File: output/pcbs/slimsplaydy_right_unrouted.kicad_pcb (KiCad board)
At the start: 2 copper layers, 122.9 x 94.7 mm, 42 parts

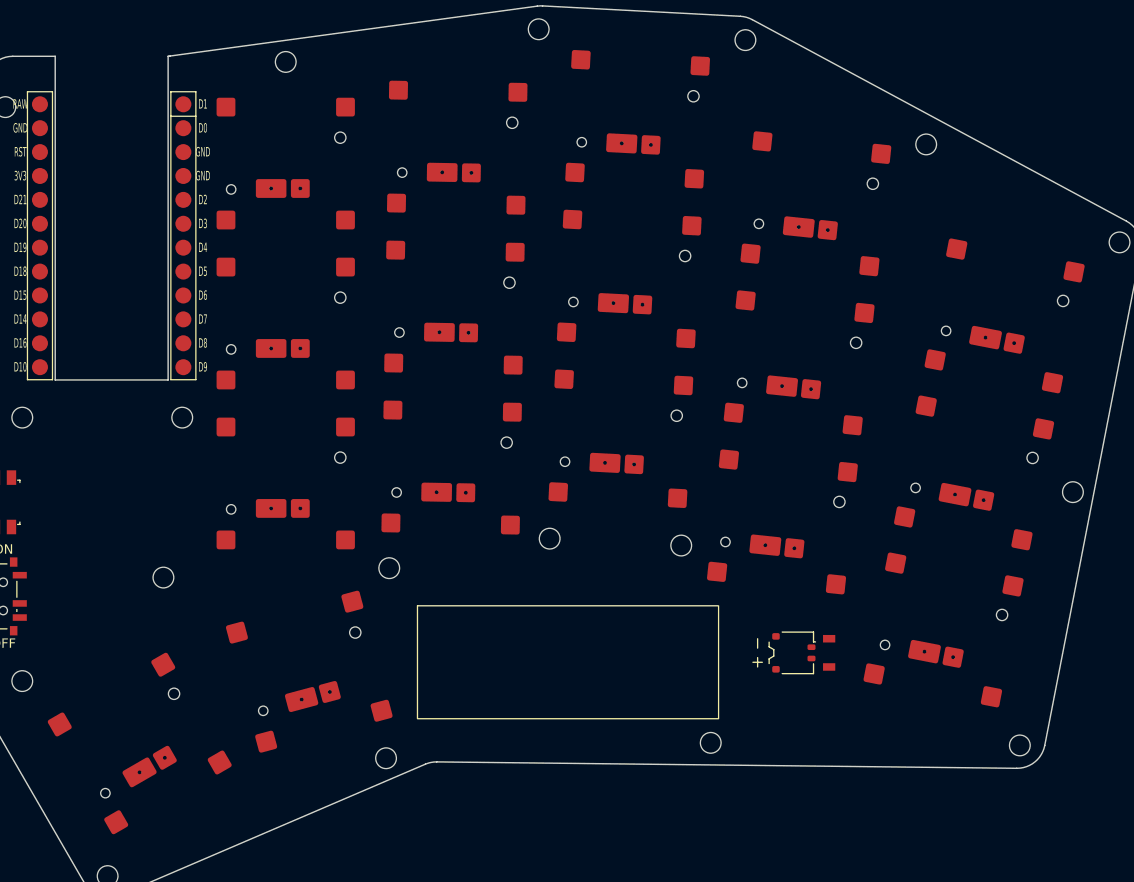
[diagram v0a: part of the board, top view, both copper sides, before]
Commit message: Add via holesize options separate from via size options.
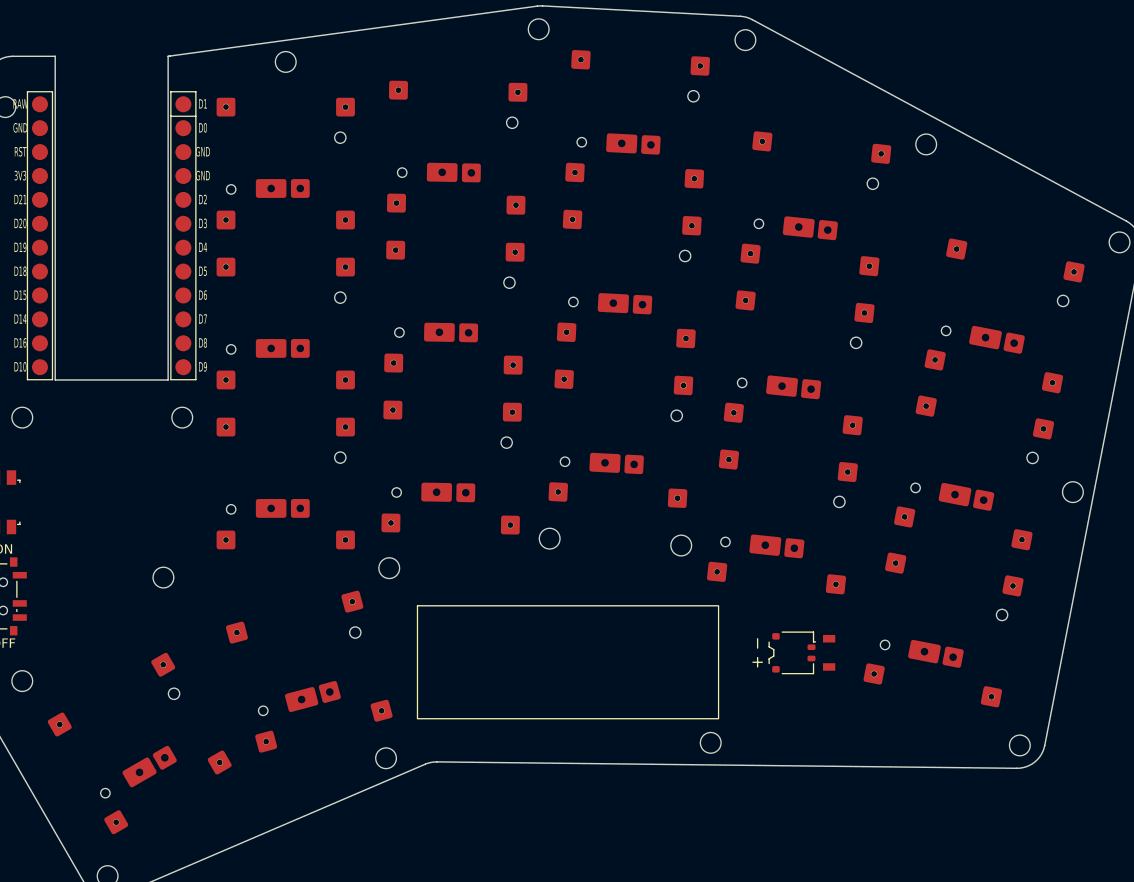
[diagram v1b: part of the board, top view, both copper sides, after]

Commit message: Finish layout, schematic, routing.
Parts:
- removed MH16, MH17, MH18: , ceoloide:mounting_hole_npth
- removed PAD1, PAD2: , SMDPad
- removed XX1: , Battery_301230
- added MAG1: , magsafe, B.Cu at (179.9, -32.5)
- CONN1: footprint ceoloide:battery_connector_molex_pico_ezmate_1x02 -> Molex_Pico_EZMate_Plus_1x02
- moved MH15 245.8 mm to (163.9, -60.5), turned to 0 degrees
- moved MH5 228.6 mm to (123.4, -55.5)
- moved MH13 219.9 mm to (240.9, -42.7), turned to -8 degrees
- moved MH14 216.9 mm to (222.0, -51.8), turned to -3 degrees
- moved MH8 208.3 mm to (123.9, 8.55), turned to 0 degrees
- moved CONN1 200.6 mm to (184.9, -8.45), turned to 0 degrees
- moved MH4 196.4 mm to (147.9, -57.8)
- moved MH6 195.1 mm to (134.9, -21.5)
- moved MH7 194.8 mm to (142.4, 0.55), turned to 0 degrees
- moved MH3 193.5 mm to (189.9, -64.8)
- moved S6 179.7 mm to (209.8, -47.4), turned to -3 degrees
- moved S5 179.1 mm to (208.9, -30.5), turned to -3 degrees
- moved S9 178.7 mm to (189.9, -54.5), turned to 0 degrees
- moved S4 178.5 mm to (208.0, -13.5), turned to -3 degrees
- moved S3 178.3 mm to (229.7, -33.7), turned to -8 degrees
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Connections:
- MCU1 pad 1: mirror_hand_middle_top -> mirror_finger_inner_home
- MCU1 pad 10: mirror_hand_inner_home -> mirror_finger_pinky_top
- MCU1 pad 11: mirror_hand_ring_home -> mirror_thumb_tucky_fan
- MCU1 pad 12: mirror_hand_pinky_home -> mirror_thumb_reachy_fan
- MCU1 pad 13: mirror_hand_pinky_bottom -> mirror_finger_index_home
- MCU1 pad 14: mirror_hand_middle_bottom -> mirror_finger_middle_home
- MCU1 pad 15: mirror_hand_index_bottom -> mirror_finger_ring_home
- MCU1 pad 16: mirror_hand_inner_bottom -> mirror_finger_pinky_home
- MCU1 pad 17: mirror_hand_ring_bottom -> mirror_finger_ring_top
- MCU1 pad 18: mirror_thumb_near_fan -> mirror_finger_middle_top
- MCU1 pad 19: mirror_thumb_far_fan -> mirror_finger_index_top
- MCU1 pad 2: mirror_hand_index_top -> D0
- MCU1 pad 20: D21 -> mirror_finger_inner_top
- MCU1 pad 5: mirror_hand_inner_top -> mirror_finger_pinky_bottom
- MCU1 pad 6: mirror_hand_ring_top -> mirror_finger_ring_bottom
- MCU1 pad 7: mirror_hand_pinky_top -> mirror_finger_middle_bottom
- MCU1 pad 8: mirror_hand_middle_home -> mirror_finger_index_bottom
- MCU1 pad 9: mirror_hand_index_home -> mirror_finger_inner_bottom
- S1 pad : GND -> (no net)
- S1 pad 1: mirror_hand_pinky_bottom -> mirror_finger_pinky_bottom
- S1 pad 3: (no net) -> GND
- S10 pad : GND -> (no net)
- S10 pad 1: mirror_hand_index_bottom -> mirror_finger_index_bottom
- S10 pad 3: (no net) -> GND
- S11 pad : GND -> (no net)
- S11 pad 1: mirror_hand_index_home -> mirror_finger_index_home
- S11 pad 3: (no net) -> GND
- S12 pad : GND -> (no net)
- S12 pad 1: mirror_hand_index_top -> mirror_finger_index_top
- S12 pad 3: (no net) -> GND
- S13 pad : GND -> (no net)
- S13 pad 1: mirror_hand_inner_bottom -> mirror_finger_inner_bottom
- S13 pad 3: (no net) -> GND
- S14 pad : GND -> (no net)
- S14 pad 1: mirror_hand_inner_home -> mirror_finger_inner_home
- S14 pad 3: (no net) -> GND
- S15 pad : GND -> (no net)
- S15 pad 1: mirror_hand_inner_top -> mirror_finger_inner_top
- S15 pad 3: (no net) -> GND
- S16 pad : GND -> (no net)
- S16 pad 1: mirror_thumb_near_fan -> mirror_thumb_tucky_fan
- S16 pad 3: (no net) -> GND
- S17 pad : GND -> (no net)
- S17 pad 1: mirror_thumb_far_fan -> mirror_thumb_reachy_fan
- S17 pad 3: (no net) -> GND
- S2 pad : GND -> (no net)
- S2 pad 1: mirror_hand_pinky_home -> mirror_finger_pinky_home
- S2 pad 3: (no net) -> GND
- S3 pad : GND -> (no net)
- S3 pad 1: mirror_hand_pinky_top -> mirror_finger_pinky_top
- S3 pad 3: (no net) -> GND
- S4 pad : GND -> (no net)
- S4 pad 1: mirror_hand_ring_bottom -> mirror_finger_ring_bottom
- S4 pad 3: (no net) -> GND
- S5 pad : GND -> (no net)
- S5 pad 1: mirror_hand_ring_home -> mirror_finger_ring_home
- S5 pad 3: (no net) -> GND
- S6 pad : GND -> (no net)
- S6 pad 1: mirror_hand_ring_top -> mirror_finger_ring_top
- S6 pad 3: (no net) -> GND
- S7 pad : GND -> (no net)
- S7 pad 1: mirror_hand_middle_bottom -> mirror_finger_middle_bottom
- S7 pad 3: (no net) -> GND
- S8 pad : GND -> (no net)
- S8 pad 1: mirror_hand_middle_home -> mirror_finger_middle_home
- S8 pad 3: (no net) -> GND
- S9 pad : GND -> (no net)
- S9 pad 1: mirror_hand_middle_top -> mirror_finger_middle_top
- S9 pad 3: (no net) -> GND
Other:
- board size 122.9 x 94.7 mm -> 122.6 x 97.5 mm

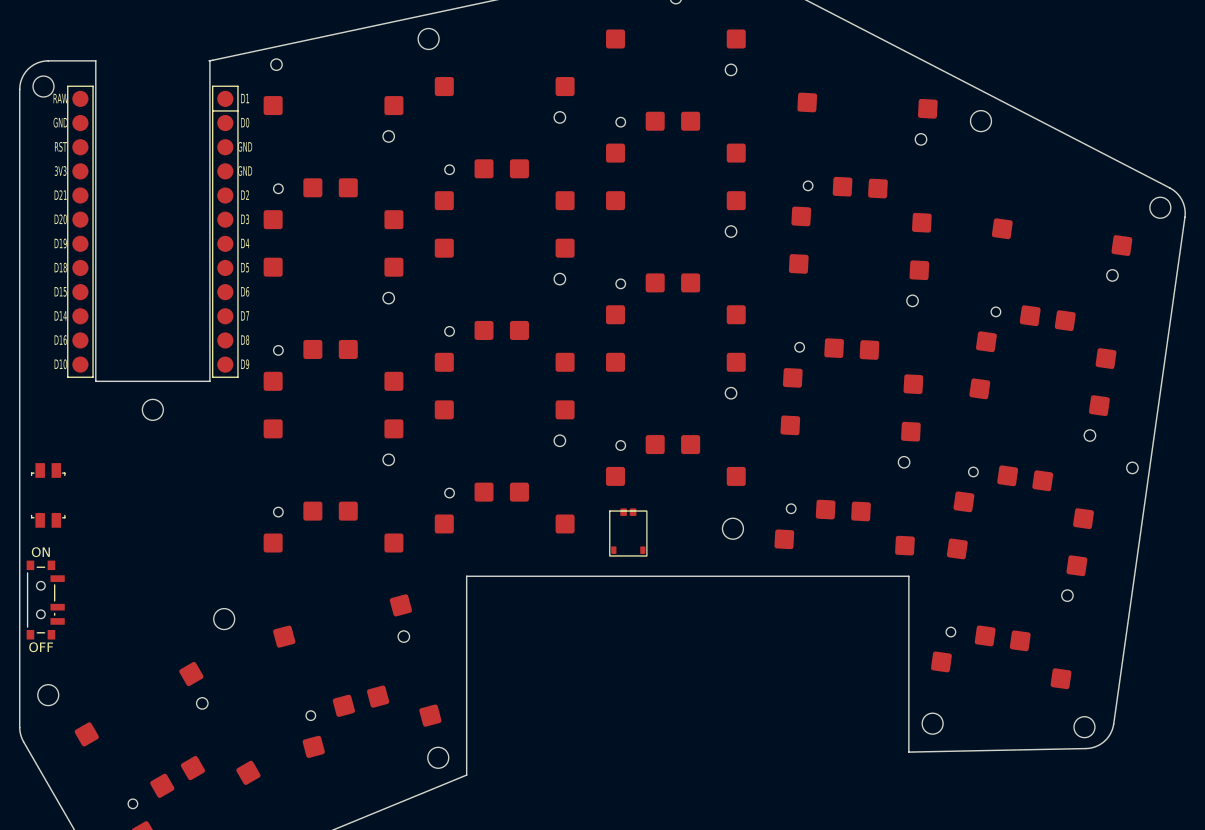
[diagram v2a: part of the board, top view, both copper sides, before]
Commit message: Fix MCU slots. Fillet outline. Reroute both sides. Re-re-reroute both sides.
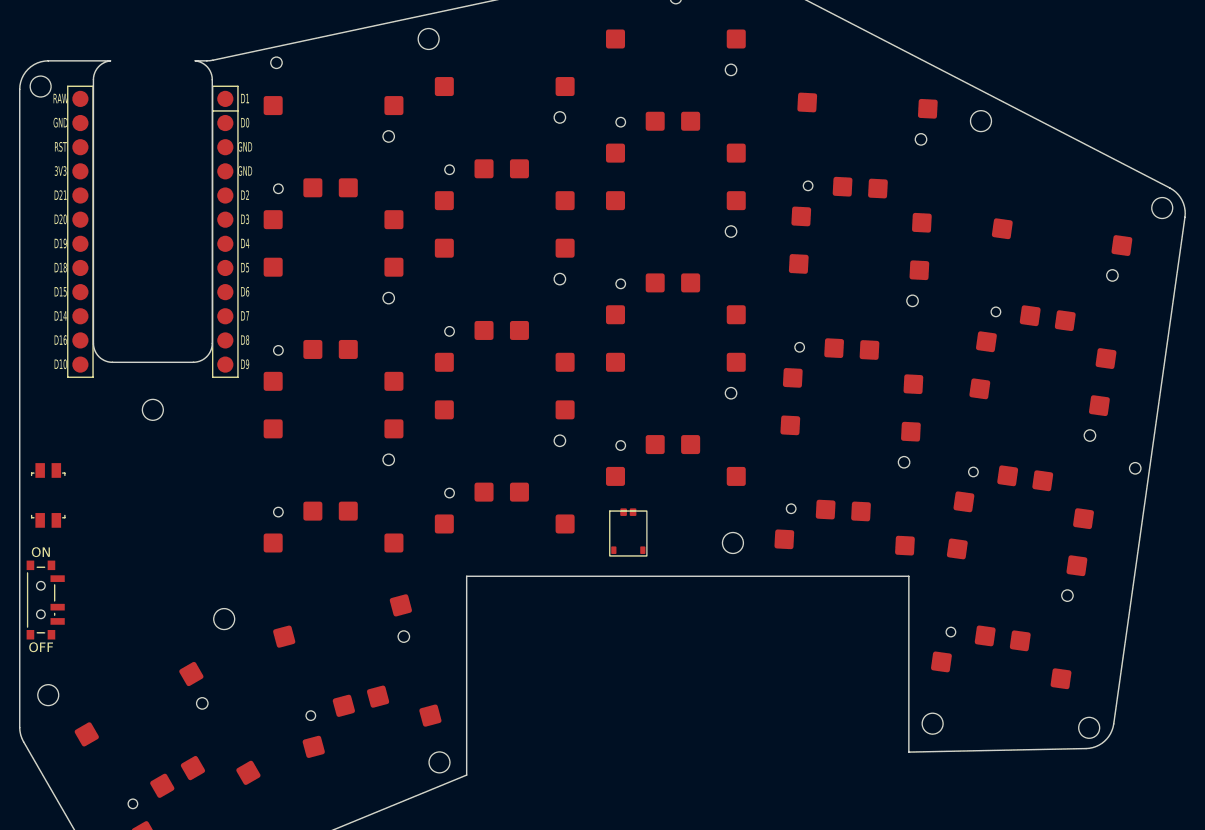
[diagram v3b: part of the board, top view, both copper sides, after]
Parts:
- moved MH10 1.50 mm to (195.9, -7.45)
- moved MH9 0.50 mm to (165.1, 15.6)
- moved MH12 0.50 mm to (233.4, 12.0)
- moved MH2 0.30 mm to (238.3, -15.3)
- moved MH5 0.30 mm to (123.1, -55.5)
- moved MH4 0.20 mm to (147.9, -58.0)
- moved MH13 0.20 mm to (241.1, -42.7)
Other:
- outline, holes or cut-outs redrawn
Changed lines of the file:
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@@
   (title_block
     (title "slimsplaydy_right_unrouted")
-    (date "2025-06-13")
+    (date "2025-06-14")
     (rev "0.1")
     (company "huntercook")
@@
   (footprint "ceoloide:mounting_hole_npth"
     (layer "F.Cu")
-    (at 237.95889780000002 -15.345405 -8)
+    (at 238.2559783 -15.303653099999998 -8)
     (property "Reference" "MH2"
       (at 0 2.55 -8)
@@
   (footprint "ceoloide:mounting_hole_npth"
     (layer "F.Cu")
-    (at 147.9492103 -57.7502446 0)
+    (at 147.9492103 -57.950244600000005 0)
     (property "Reference" "MH4"
       (at 0 2.55 0)
@@
   (footprint "ceoloide:mounting_hole_npth"
     (layer "F.Cu")
-    (at 123.4492103 -55.450244600000005 0)
+    (at 123.14921030000001 -55.450244600000005 0)
     (property "Reference" "MH5"
       (at 0 2.55 0)
@@
   (footprint "ceoloide:mounting_hole_npth"
     (layer "F.Cu")
-    (at 164.96236520000002 15.139062299999999 15)
+    (at 165.0917748 15.6220252 15)
     (property "Reference" "MH9"
       (at 0 2.55 15)
@@
   (footprint "ceoloide:mounting_hole_npth"
     (layer "F.Cu")
-    (at 195.9492104 -8.9502445 0)
+    (at 195.9492104 -7.4502445 0)
     (property "Reference" "MH10"
       (at 0 2.55 0)
@@
   (footprint "ceoloide:mounting_hole_npth"
     (layer "F.Cu")
-    (at 232.9154813 11.9180128 -8)
+    (at 233.41061530000002 11.9875993 -8)
     (property "Reference" "MH12"
       (at 0 2.55 -8)
@@
   (footprint "ceoloide:mounting_hole_npth"
     (layer "F.Cu")
-    (at 240.8949168 -42.703032699999994 -8)
+    (at 241.0929704 -42.675198099999996 -8)
     (property "Reference" "MH13"
       (at 0 2.55 -8)
@@
 (gr_line (start 199.2201997686415 -66.4502445) (end 180.26490610994585 -66.4502445) (layer Edge.Cuts) (stroke (width 0.15) (type default)))
 (gr_line (start 179.64043003030574 -66.384529704333) (end 141.25799066969427 -58.215959395667) (layer Edge.Cuts) (stroke (width 0.15) (type default)))
-(gr_line (start 128.9492103 -58.15024460000001) (end 123.9492103 -58.15024460000001) (layer Edge.Cuts) (stroke (width 0.15) (type default)))
+(gr_line (start 140.63351459005412 -58.15024460000001) (end 139.3989601 -58.15024460000001) (layer Edge.Cuts) (stroke (width 0.15) (type default)))
+(gr_line (start 130.4994605 -58.15024460000001) (end 123.9492103 -58.15024460000001) (layer Edge.Cuts) (stroke (width 0.15) (type default)))
 (gr_line (start 120.9492103 -55.15024460000001) (end 120.9492103 11.946543806493537) (layer Edge.Cuts) (stroke (width 0.15) (type default)))
 (gr_arc (start 130.61138423458036 29.500431777802792) (mid 132.24169433458036 30.840875077802792) (end 134.35130993458037 30.77590247780279) (layer Edge.Cuts) (stroke (width 0.15) (type default)))
@@
 (gr_arc (start 200.59692436864148 -66.1156956) (mid 199.9285946686415 -66.3654078) (end 199.2201997686415 -66.4502445) (layer Edge.Cuts) (stroke (width 0.15) (type default)))
 (gr_arc (start 180.26490610994585 -66.4502445) (mid 179.95094400994586 -66.4337706) (end 179.64043000994585 -66.3845297) (layer Edge.Cuts) (stroke (width 0.15) (type default)))
-(gr_arc (start 140.87825939005413 -58.160244600000006) (mid 141.06901689005412 -58.182023300000004) (end 141.25799069005413 -58.21595940000001) (layer Edge.Cuts) (stroke (width 0.15) (type default)))
+(gr_arc (start 140.63351459005412 -58.15024460000001) (mid 140.94747669005412 -58.16671850000001) (end 141.25799069005413 -58.21595940000001) (layer Edge.Cuts) (stroke (width 0.15) (type default)))
 (gr_arc (start 123.9492103 -58.15024460000001) (mid 121.82789000000001 -57.27156490000001) (end 120.9492103 -55.15024460000001) (layer Edge.Cuts) (stroke (width 0.15) (type default)))
 (gr_arc (start 120.9492103 11.946543806493537) (mid 121.0512793 12.722427806493537) (end 121.350541 13.445516006493538) (layer Edge.Cuts) (stroke (width 0.15) (type default)))
-(gr_line (start 140.87825939005413 -58.160244600000006) (end 140.9492103 -58.160244600000006) (layer Edge.Cuts) (stroke (width 0.15) (type default)))
-(gr_line (start 140.9492103 -58.160244600000006) (end 140.9492103 -24.450244600000005) (layer Edge.Cuts) (stroke (width 0.15) (type default)))
-(gr_line (start 140.9492103 -24.450244600000005) (end 128.9492103 -24.450244600000005) (layer Edge.Cuts) (stroke (width 0.15) (type default)))
-(gr_line (start 128.9492103 -24.450244600000005) (end 128.9492103 -58.15024460000001) (layer Edge.Cuts) (stroke (width 0.15) (type default)))
+(gr_line (start 141.1992103 -56.160244600000006) (end 141.1992103 -28.450244600000005) (layer Edge.Cuts) (stroke (width 0.15) (type default)))
+(gr_line (start 139.1992103 -26.450244600000005) (end 130.6992103 -26.450244600000005) (layer Edge.Cuts) (stroke (width 0.15) (type default)))
+(gr_line (start 128.6992103 -28.450244600000005) (end 128.6992103 -56.160244600000006) (layer Edge.Cuts) (stroke (width 0.15) (type default)))
+(gr_arc (start 141.1992103 -56.160244600000006) (mid 140.6823657 -57.50197860000001) (end 139.3989601 -58.15024460000001) (layer Edge.Cuts) (stroke (width 0.15) (type default)))
+(gr_arc (start 139.1992103 -26.450244600000005) (mid 140.61342390000002 -27.036031000000005) (end 141.1992103 -28.450244600000005) (layer Edge.Cuts) (stroke (width 0.15) (type default)))
+(gr_arc (start 128.6992103 -28.450244600000005) (mid 129.2849967 -27.036031000000005) (end 130.6992103 -26.450244600000005) (layer Edge.Cuts) (stroke (width 0.15) (type default)))
+(gr_arc (start 130.4994605 -58.15024460000001) (mid 129.216055 -57.50197860000001) (end 128.6992103 -56.160244600000006) (layer Edge.Cuts) (stroke (width 0.15) (type default)))
 (gr_line (start 214.4492104 14.539434268083982) (end 214.4492104 -3.9502445) (layer Edge.Cuts) (stroke (width 0.15) (type default)))
 (gr_line (start 214.4492104 -3.9502445) (end 167.9492104 -3.9502445) (layer Edge.Cuts) (stroke (width 0.15) (type default)))

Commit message: Add production files.
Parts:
- moved MCU1 0.20 mm to (134.9, -41.7)
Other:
- outline, holes or cut-outs redrawn
